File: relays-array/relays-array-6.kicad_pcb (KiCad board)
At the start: 2 copper layers, 173 x 60 mm, 50 parts, among them J1 NMJ6HCD2, J10 Screw_Terminal_01x02, J14 NMJ6HCD2, J15 Screw_Terminal_01x02, J2 NMJ6HCD2, J3 Screw_Terminal_01x02, J4 NMJ6HCD2, J5 NMJ6HCD2, J6 Screw_Terminal_01x02, J7 NMJ6HCD2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

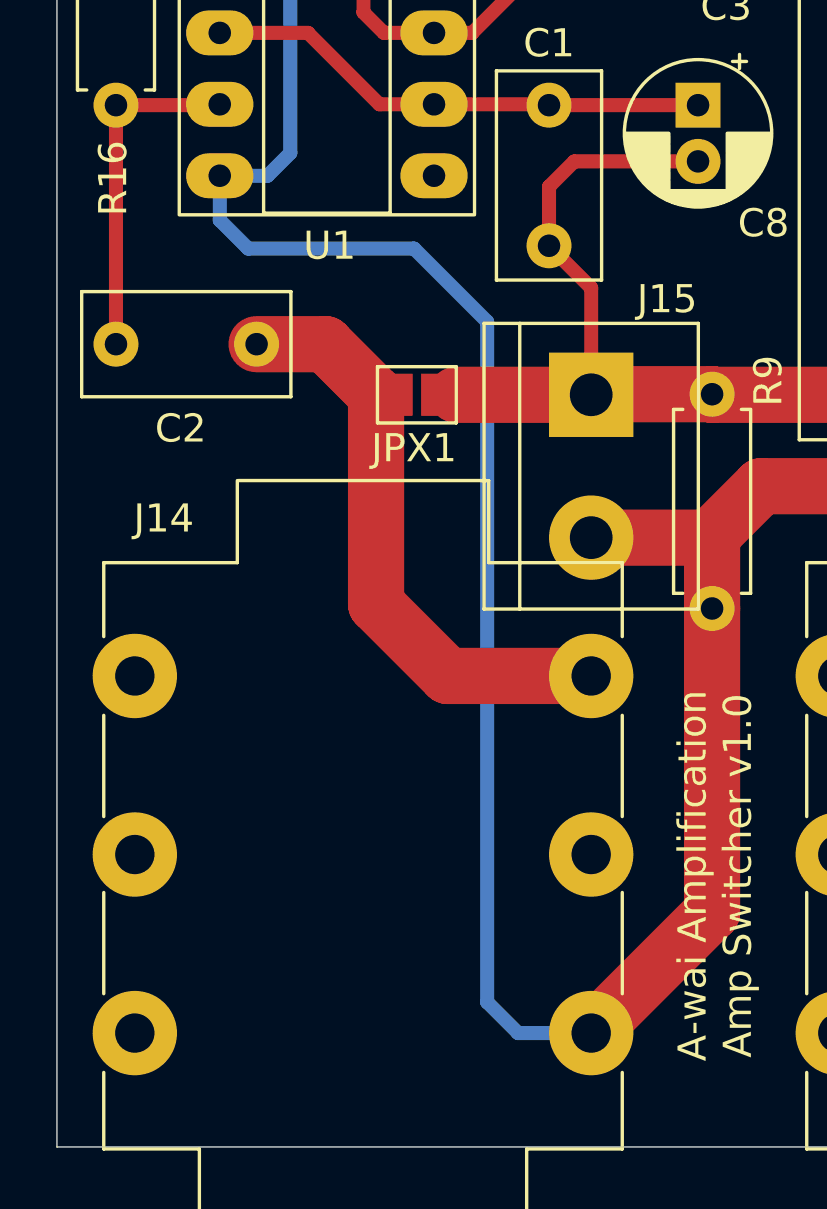
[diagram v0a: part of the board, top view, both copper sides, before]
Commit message: relays-array: add terminal block for buffer use w/ external connector
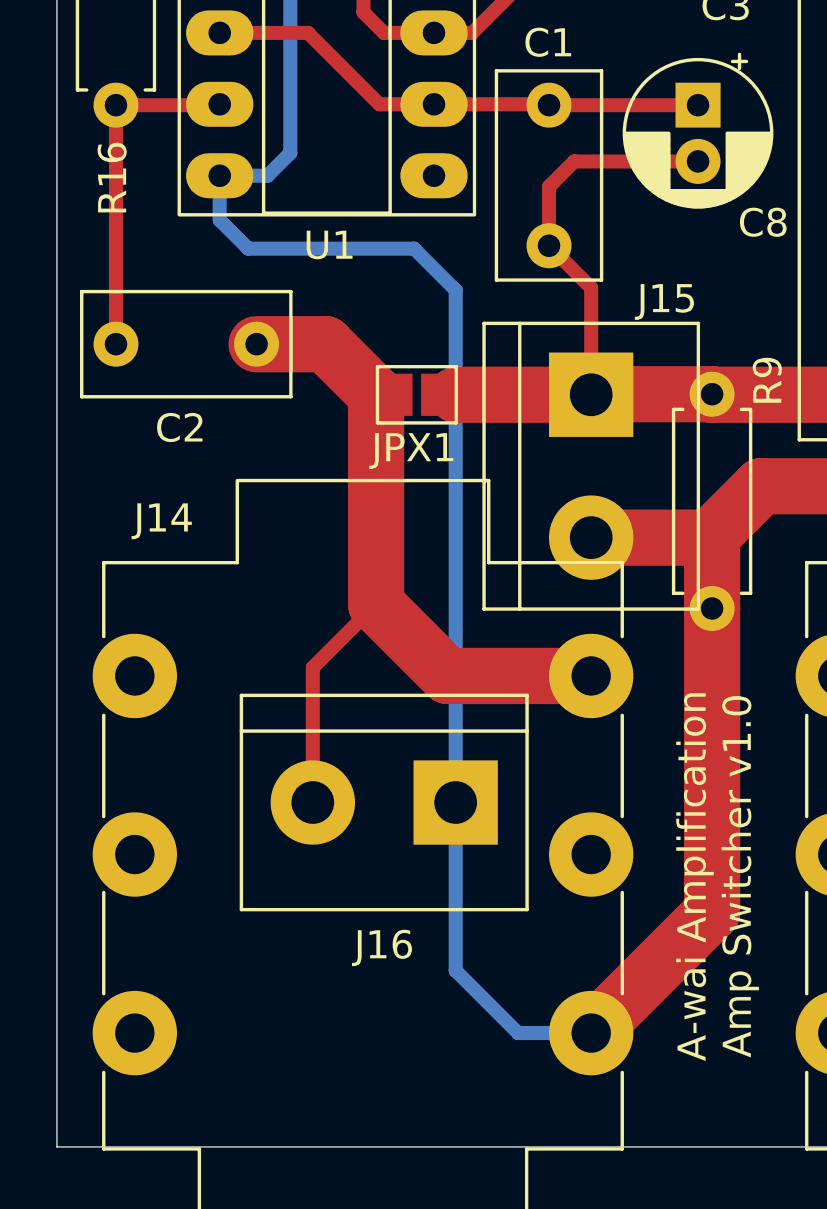
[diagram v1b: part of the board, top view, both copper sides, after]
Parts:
- added J16: Screw_Terminal_01x02, TerminalBlock:TerminalBlock_bornier-2_P5.08mm, F.Cu at (50.2, 114.5)
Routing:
- net Net-(J16-Pin_2): track 21.2 -> 29.1 mm

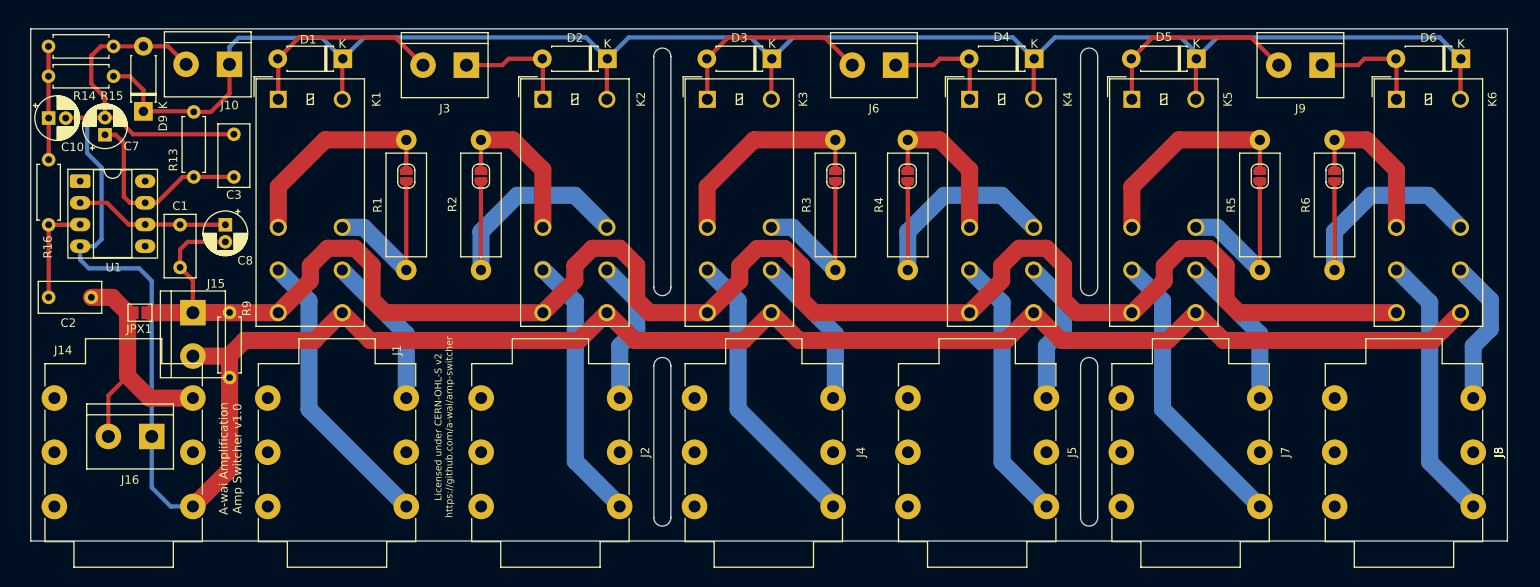
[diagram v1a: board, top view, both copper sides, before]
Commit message: relays-array: add terminal block labels on silkscreen
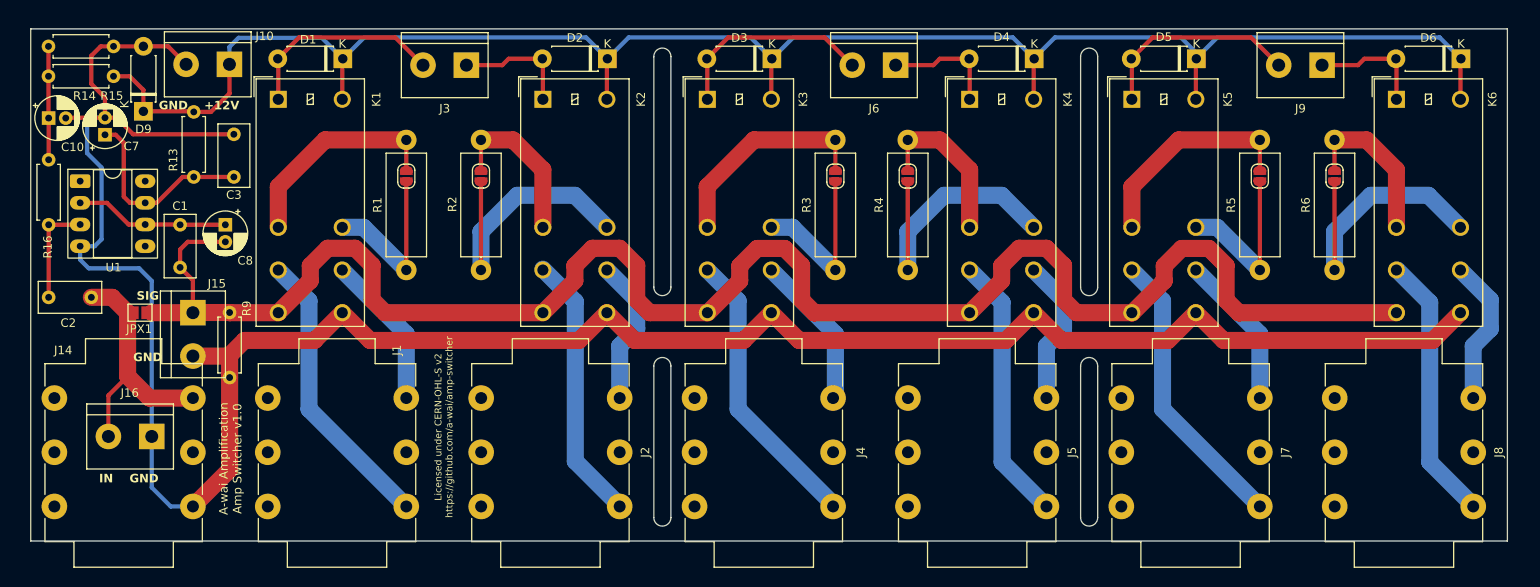
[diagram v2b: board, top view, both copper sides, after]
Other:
- board text added: "GND"
- board text added: "GND +12V"
- board text added: "IN GND"
- board text added: "SIG"
- board text removed: "J5"
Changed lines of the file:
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@@
 		(tags "terminal block bornier2")
 		(property "Reference" "J16"
-			(at 2.54 -5.08 0)
+			(at 2.58 5.1 0)
 			(layer "F.SilkS")
 			(effects
@@
 		(tags "Diode DO-41_SOD81 series Axial Horizontal pin pitch 7.62mm  length 5.2mm diameter 2.7mm")
 		(property "Reference" "D9"
-			(at -1.39 2.3 90)
+			(at -2.09 0 180)
 			(layer "F.SilkS")
 			(effects
@@
 		)
 		(fp_text user "K"
-			(at 0.71 2.3 90)
+			(at 0.81 -2.2 90)
 			(layer "F.SilkS")
 			(effects
@@
 		(tags "terminal block bornier2")
 		(property "Reference" "J15"
-			(at -3.4 -2.7 0)
+			(at -3.4 -2.8 0)
 			(layer "F.SilkS")
 			(effects
@@
 		(tags "terminal block bornier2")
 		(property "Reference" "J10"
-			(at -0.02 -4.8 0)
+			(at -4.12 3.3 0)
 			(layer "F.SilkS")
 			(effects
@@
 		(layer "Edge.Cuts")
 	)
+	(gr_text "GND"
+		(at 48 105.8 0)
+		(layer "F.SilkS")
+		(effects
+			(font
+				(size 1 1)
+				(thickness 0.2)
+				(bold yes)
+			)
+			(justify left bottom)
+		)
+	)
+	(gr_text "GND    +12V"
+		(at 51 76.3 0)
+		(layer "F.SilkS")
+		(effects
+			(font
+				(size 1 1)
+				(thickness 0.2)
+				(bold yes)
+			)
+			(justify left bottom)
+		)
+	)
 	(gr_text "Licensed under CERN-OHL-S v2\nhttps://github.com/a-wai/amp-switcher"
 		(at 85.5 113.4 90)
@@
 		)
 	)
+	(gr_text "IN    GND"
+		(at 44 120 0)
+		(layer "F.SilkS")
+		(effects
+			(font
+				(size 1 1)
+				(thickness 0.2)
+				(bold yes)
+			)
+			(justify left bottom)
+		)
+	)
 	(gr_text "A-wai Amplification\nAmp Switcher v1.0"
 		(at 60.8 117.1 90)
@@
 		)
 	)
-	(gr_text "J5"
-		(at 208 116.35 90)
+	(gr_text "SIG"
+		(at 48.4 98.6 0)
 		(layer "F.SilkS")
 		(effects
 			(font
 				(size 1 1)
-				(thickness 0.15)
+				(thickness 0.2)
+				(bold yes)
 			)
+			(justify left bottom)
 		)
 	)

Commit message: relays-array: fix schematics error and add ground plane
The jack connectors are all (except for the buffer input) wired
backwards, with the tip going to `GND` and the sleeve on `SIGNAL`, while
it should be the other way around.

While at it, improve a bit the PCB tracks and add a ground plane. The
latter is only connected to `GND` in a single point in order to avoid
ground loops and other unpleasant issues.
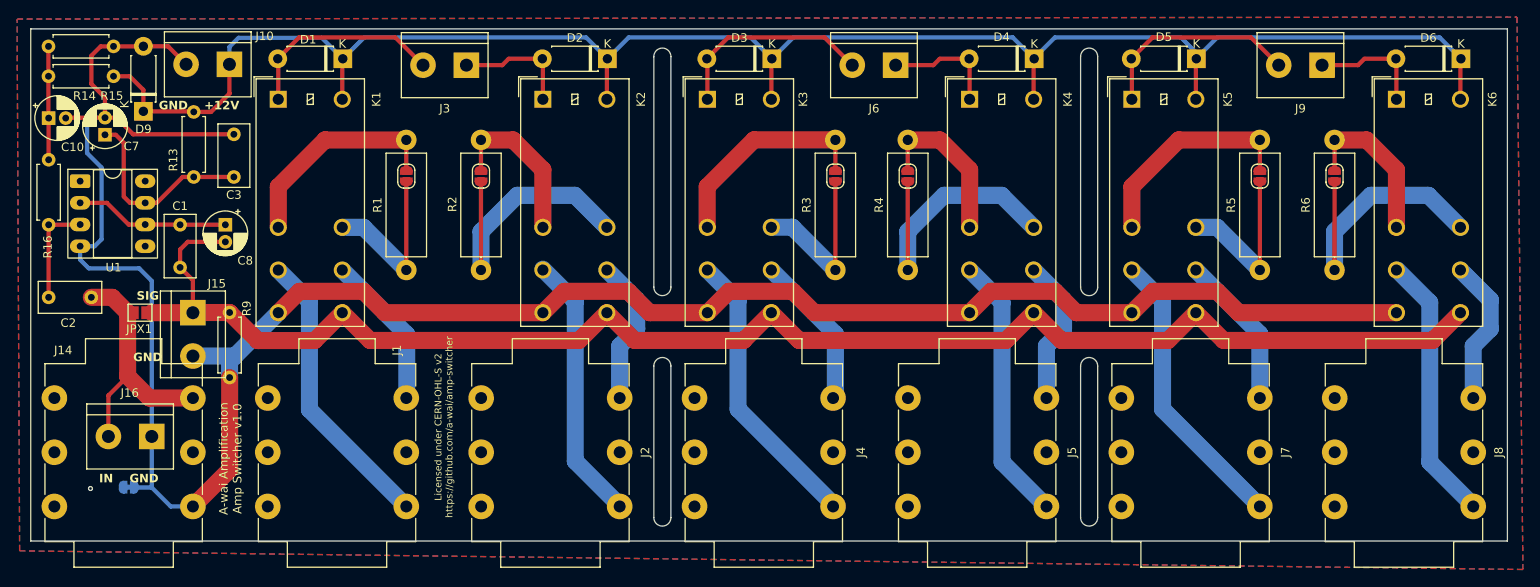
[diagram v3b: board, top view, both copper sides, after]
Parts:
- added JP1: Jumper_2_Bridged, Jumper:SolderJumper-2_P1.3mm_Bridged_RoundedPad1.0x1.5mm, B.Cu at (47.5, 120.4)
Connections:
- K1 pad 14: /SIGNAL -> GND
- K1 pad 24: GND -> /SIGNAL
- K2 pad 14: /SIGNAL -> GND
- K2 pad 24: GND -> /SIGNAL
- K3 pad 14: /SIGNAL -> GND
- K3 pad 24: GND -> /SIGNAL
- K4 pad 14: /SIGNAL -> GND
- K4 pad 24: GND -> /SIGNAL
- K5 pad 14: /SIGNAL -> GND
- K5 pad 24: GND -> /SIGNAL
- K6 pad 14: /SIGNAL -> GND
- K6 pad 24: GND -> /SIGNAL
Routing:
- net /SIGNAL: track 207.8 -> 183.2 mm
- net GND: track 284.8 -> 276.5 mm
- net Earth: vias 0 -> 1
- added copper zone on B.Cu, net Earth
- added copper zone on F.Cu, net Earth
